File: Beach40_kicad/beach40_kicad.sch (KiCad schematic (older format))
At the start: 75 parts, among them K1 RELAY_2RT, P1 LO In, P2 Mic In, P3 Audio Out, P4 ANT, Q1 BC548, Q2 2N2222, Q3 BD139, Q4 BD139, U1 LM386

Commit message: - slight fixes, working on 2 computers now!
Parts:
- C1, C20, C21, C23, C3, C4, C8: footprint FT:1210_CAP -> Capacitors_ThroughHole:Capacitor3MMDiscRM2.5
- C10, C26: footprint (none) -> FT:CAP_ELECTRO_D4S1.8
- C11, C13, C14, C15, C16, C17, C18, C19, C22, C24, C25, C27, C28, C29: footprint (none) -> Capacitors_ThroughHole:Capacitor3MMDiscRM2.5
- C12: value C_POL -> 220u; footprint (none) -> FT:CAP_ELECTRO_D4S1.8
- C2: value CAP -> 100n; footprint FT:1210_CAP -> Capacitors_ThroughHole:Capacitor3MMDiscRM2.5
- C5: value C_POL -> 1u
- C7, C9: footprint FT:1210_CAP -> FT:CAP_ELECTRO_D4S1.8
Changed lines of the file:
@@
 EESchema Schematic File Version 2
-LIBS:freetronics_schematic
 LIBS:sma
 LIBS:power
@@
 LIBS:atmel
 LIBS:contrib
-LIBS:sma_edge
 LIBS:valves
 LIBS:beach40_kicad-cache
@@
 F 0 "C8" H 3250 5850 40  0000 L CNN
 F 1 "10nF" H 3256 5665 40  0000 L CNN
-F 2 "FT:1210_CAP" H 3288 5600 30  0001 C CNN
+F 2 "Capacitors_ThroughHole:Capacitor3MMDiscRM2.5" H 3288 5600 30  0001 C CNN
 F 3 "" H 3250 5750 60  0000 C CNN
 	1    3250 5750
@@
 F 3 "" H 6150 4050 60  0000 C CNN
 	1    6150 4050
-	1    0    0    -1
+	0    -1   -1   0
 $EndComp
 $Comp
@@
 F 3 "" H 6150 3600 60  0000 C CNN
 	1    6150 3600
-	1    0    0    -1
+	0    -1   -1   0
 $EndComp
 Wire Wire Line
@@
 F 0 "C14" H 5400 3700 50  0000 L CNN
 F 1 "100n" H 5400 3500 50  0000 L CNN
-F 2 "" H 5350 3600 60  0001 C CNN
+F 2 "Capacitors_ThroughHole:Capacitor3MMDiscRM2.5" H 5350 3600 60  0001 C CNN
 F 3 "" H 5350 3600 60  0000 C CNN
 	1    5350 3600
@@
 F 0 "C20" H 7000 4300 50  0000 L CNN
 F 1 "100n" H 7000 4100 50  0000 L CNN
-F 2 "FT:1210_CAP" H 6950 4200 60  0001 C CNN
+F 2 "Capacitors_ThroughHole:Capacitor3MMDiscRM2.5" H 6950 4200 60  0001 C CNN
 F 3 "" H 6950 4200 60  0000 C CNN
 	1    6950 4200
@@
 F 0 "C23" H 7850 6000 50  0000 L CNN
 F 1 "100n" H 7850 5800 50  0000 L CNN
-F 2 "FT:1210_CAP" H 7800 5900 60  0001 C CNN
+F 2 "Capacitors_ThroughHole:Capacitor3MMDiscRM2.5" H 7800 5900 60  0001 C CNN
 F 3 "" H 7800 5900 60  0000 C CNN
 	1    7800 5900
@@
 F 3 "" H 7800 4350 60  0000 C CNN
 	1    7800 4350
-	1    0    0    -1
+	0    -1   -1   0
 $EndComp
 $Comp
@@
 F 3 "" H 7800 4000 60  0000 C CNN
 	1    7800 4000
-	1    0    0    -1
+	0    -1   -1   0
 $EndComp
 Wire Wire Line
@@
 F 0 "C21" H 7400 3800 50  0000 L CNN
 F 1 "100n" H 7400 3600 50  0000 L CNN
-F 2 "FT:1210_CAP" H 7350 3700 60  0001 C CNN
+F 2 "Capacitors_ThroughHole:Capacitor3MMDiscRM2.5" H 7350 3700 60  0001 C CNN
 F 3 "" H 7350 3700 60  0000 C CNN
 	1    7350 3700
@@
 F 0 "C15" H 5400 4550 50  0000 L CNN
 F 1 "1n" H 5400 4350 50  0000 L CNN
-F 2 "" H 5350 4450 60  0001 C CNN
+F 2 "Capacitors_ThroughHole:Capacitor3MMDiscRM2.5" H 5350 4450 60  0001 C CNN
 F 3 "" H 5350 4450 60  0000 C CNN
 	1    5350 4450
@@
 F 0 "C3" H 2350 5100 50  0000 L CNN
 F 1 "10n" H 2350 4900 50  0000 L CNN
-F 2 "FT:1210_CAP" H 2300 5000 60  0001 C CNN
+F 2 "Capacitors_ThroughHole:Capacitor3MMDiscRM2.5" H 2300 5000 60  0001 C CNN
 F 3 "" H 2300 5000 60  0000 C CNN
 	1    2300 5000
@@
 F 0 "C16" H 5700 5000 50  0000 L CNN
 F 1 "100n" H 5700 4800 50  0000 L CNN
-F 2 "" H 5650 4900 60  0001 C CNN
+F 2 "Capacitors_ThroughHole:Capacitor3MMDiscRM2.5" H 5650 4900 60  0001 C CNN
 F 3 "" H 5650 4900 60  0000 C CNN
 	1    5650 4900
@@
 F 0 "C17" H 6650 6150 50  0000 L CNN
 F 1 "100n" H 6650 5950 50  0000 L CNN
-F 2 "" H 6600 6050 60  0001 C CNN
+F 2 "Capacitors_ThroughHole:Capacitor3MMDiscRM2.5" H 6600 6050 60  0001 C CNN
 F 3 "" H 6600 6050 60  0000 C CNN
 	1    6600 6050
@@
 F 0 "C25" H 8350 4300 50  0000 L CNN
 F 1 "100n" H 8350 4100 50  0000 L CNN
-F 2 "" H 8300 4200 60  0001 C CNN
+F 2 "Capacitors_ThroughHole:Capacitor3MMDiscRM2.5" H 8300 4200 60  0001 C CNN
 F 3 "" H 8300 4200 60  0000 C CNN
 	1    8300 4200
@@
 F 3 "" H 8900 3800 60  0000 C CNN
 	1    8900 3800
-	0    1    1    0
+	-1   0    0    1
 $EndComp
 Wire Wire Line
@@
 F 0 "C29" H 9400 4200 50  0000 L CNN
 F 1 "100n" H 9400 4000 50  0000 L CNN
-F 2 "" H 9350 4100 60  0001 C CNN
+F 2 "Capacitors_ThroughHole:Capacitor3MMDiscRM2.5" H 9350 4100 60  0001 C CNN
 F 3 "" H 9350 4100 60  0000 C CNN
 	1    9350 4100
@@
 F 0 "C26" H 8600 3600 50  0000 L CNN
 F 1 "220u" H 8600 3400 50  0000 L CNN
-F 2 "" H 8550 3500 60  0001 C CNN
+F 2 "FT:CAP_ELECTRO_D4S1.8" H 8550 3500 60  0001 C CNN
 F 3 "" H 8550 3500 60  0000 C CNN
 	1    8550 3500
@@
 F 3 "" H 7250 2150 60  0000 C CNN
 	1    7250 2150
-	1    0    0    -1
+	0    -1   -1   0
 $EndComp
 $Comp
@@
 F 3 "" H 7900 2150 60  0000 C CNN
 	1    7900 2150
-	1    0    0    -1
+	0    -1   -1   0
 $EndComp
 $Comp
@@
 F 3 "" H 8550 2150 60  0000 C CNN
 	1    8550 2150
-	1    0    0    -1
+	0    -1   -1   0
 $EndComp
 Text GLabel 6800 2150 0    60   Input ~ 0
@@
 F 0 "C19" H 7000 2550 50  0000 L CNN
 F 1 "220p" H 7000 2350 50  0000 L CNN
-F 2 "" H 6950 2450 60  0001 C CNN
+F 2 "Capacitors_ThroughHole:Capacitor3MMDiscRM2.5" H 6950 2450 60  0001 C CNN
 F 3 "" H 6950 2450 60  0000 C CNN
 	1    6950 2450
@@
 F 0 "C18" H 6750 2550 50  0000 L CNN
 F 1 "220p" H 6750 2350 50  0000 L CNN
-F 2 "" H 6700 2450 60  0001 C CNN
+F 2 "Capacitors_ThroughHole:Capacitor3MMDiscRM2.5" H 6700 2450 60  0001 C CNN
 F 3 "" H 6700 2450 60  0000 C CNN
 	1    6700 2450
@@
 F 0 "C22" H 7500 2550 50  0000 L CNN
 F 1 "820p" H 7500 2350 50  0000 L CNN
-F 2 "" H 7450 2450 60  0001 C CNN
+F 2 "Capacitors_ThroughHole:Capacitor3MMDiscRM2.5" H 7450 2450 60  0001 C CNN
 F 3 "" H 7450 2450 60  0000 C CNN
 	1    7450 2450
@@
 F 0 "C24" H 8100 2550 50  0000 L CNN
 F 1 "820p" H 8100 2350 50  0000 L CNN
-F 2 "" H 8050 2450 60  0001 C CNN
+F 2 "Capacitors_ThroughHole:Capacitor3MMDiscRM2.5" H 8050 2450 60  0001 C CNN
 F 3 "" H 8050 2450 60  0000 C CNN
 	1    8050 2450
@@
 F 0 "C27" H 8800 2550 50  0000 L CNN
 F 1 "220p" H 8800 2350 50  0000 L CNN
-F 2 "" H 8750 2450 60  0001 C CNN
+F 2 "Capacitors_ThroughHole:Capacitor3MMDiscRM2.5" H 8750 2450 60  0001 C CNN
 F 3 "" H 8750 2450 60  0000 C CNN
 	1    8750 2450
@@
 F 0 "C28" H 9100 2550 50  0000 L CNN
 F 1 "220p" H 9100 2350 50  0000 L CNN
-F 2 "" H 9050 2450 60  0001 C CNN
+F 2 "Capacitors_ThroughHole:Capacitor3MMDiscRM2.5" H 9050 2450 60  0001 C CNN
 F 3 "" H 9050 2450 60  0000 C CNN
 	1    9050 2450
@@
 F 3 "" H 8550 1700 60  0000 C CNN
 	1    8550 1700
-	1    0    0    -1
+	0    -1   -1   0
 $EndComp
 Wire Wire Line
@@
 F 0 "C7" H 3200 1700 50  0000 L CNN
 F 1 "4.7u" H 3200 1500 50  0000 L CNN
-F 2 "FT:1210_CAP" H 3150 1600 60  0001 C CNN
+F 2 "FT:CAP_ELECTRO_D4S1.8" H 3150 1600 60  0001 C CNN
 F 3 "" H 3150 1600 60  0000 C CNN
 	1    3150 1600
@@
 F 0 "C11" H 4250 2500 50  0000 L CNN
 F 1 "4.7n" H 4250 2300 50  0000 L CNN
-F 2 "" H 4200 2400 60  0001 C CNN
+F 2 "Capacitors_ThroughHole:Capacitor3MMDiscRM2.5" H 4200 2400 60  0001 C CNN
 F 3 "" H 4200 2400 60  0000 C CNN
 	1    4200 2400
@@
 F 0 "C13" H 4950 3200 50  0000 L CNN
 F 1 "100n" H 4950 3000 50  0000 L CNN
-F 2 "" H 4900 3100 60  0001 C CNN
+F 2 "Capacitors_ThroughHole:Capacitor3MMDiscRM2.5" H 4900 3100 60  0001 C CNN
 F 3 "" H 4900 3100 60  0000 C CNN
 	1    4900 3100
@@
 F 0 "C9" H 3750 1000 50  0000 L CNN
 F 1 "220u" H 3750 800 50  0000 L CNN
-F 2 "FT:1210_CAP" H 3700 900 60  0001 C CNN
+F 2 "FT:CAP_ELECTRO_D4S1.8" H 3700 900 60  0001 C CNN
 F 3 "" H 3700 900 60  0000 C CNN
 	1    3700 900
@@
 F 0 "C10" H 4250 1500 50  0000 L CNN
 F 1 "220u" H 4250 1300 50  0000 L CNN
-F 2 "" H 4200 1400 60  0001 C CNN
+F 2 "FT:CAP_ELECTRO_D4S1.8" H 4200 1400 60  0001 C CNN
 F 3 "" H 4200 1400 60  0000 C CNN
 	1    4200 1400
@@
 P 4700 1900
 F 0 "C12" H 4750 2000 50  0000 L CNN
-F 1 "C_POL" H 4750 1800 50  0000 L CNN
-F 2 "" H 4700 1900 60  0001 C CNN
+F 1 "220u" H 4750 1800 50  0000 L CNN
+F 2 "FT:CAP_ELECTRO_D4S1.8" H 4700 1900 60  0001 C CNN
 F 3 "" H 4700 1900 60  0000 C CNN
 	1    4700 1900
@@
 P 2800 1600
 F 0 "C5" H 2850 1700 50  0000 L CNN
-F 1 "C_POL" H 2850 1500 50  0000 L CNN
+F 1 "1u" H 2850 1500 50  0000 L CNN
 F 2 "FT:CAP_ELECTRO_D4S1.8" H 2800 1600 60  0001 C CNN
 F 3 "" H 2800 1600 60  0000 C CNN
@@
 P 2300 2300
 F 0 "C2" H 2350 2400 50  0000 L CNN
-F 1 "CAP" H 2350 2200 50  0000 L CNN
-F 2 "FT:1210_CAP" H 2300 2300 60  0001 C CNN
+F 1 "100n" H 2350 2200 50  0000 L CNN
+F 2 "Capacitors_ThroughHole:Capacitor3MMDiscRM2.5" H 2300 2300 60  0001 C CNN
 F 3 "" H 2300 2300 60  0000 C CNN
 	1    2300 2300
@@
 F 0 "C4" H 2550 2600 50  0000 L CNN
 F 1 "1n" H 2550 2400 50  0000 L CNN
-F 2 "FT:1210_CAP" H 2500 2500 60  0001 C CNN
+F 2 "Capacitors_ThroughHole:Capacitor3MMDiscRM2.5" H 2500 2500 60  0001 C CNN
 F 3 "" H 2500 2500 60  0000 C CNN
 	1    2500 2500
@@
 F 0 "C1" H 2050 1450 50  0000 L CNN
 F 1 "100n" H 2050 1250 50  0000 L CNN
-F 2 "FT:1210_CAP" H 2000 1350 60  0001 C CNN
+F 2 "Capacitors_ThroughHole:Capacitor3MMDiscRM2.5" H 2000 1350 60  0001 C CNN
 F 3 "" H 2000 1350 60  0000 C CNN
 	1    2000 1350

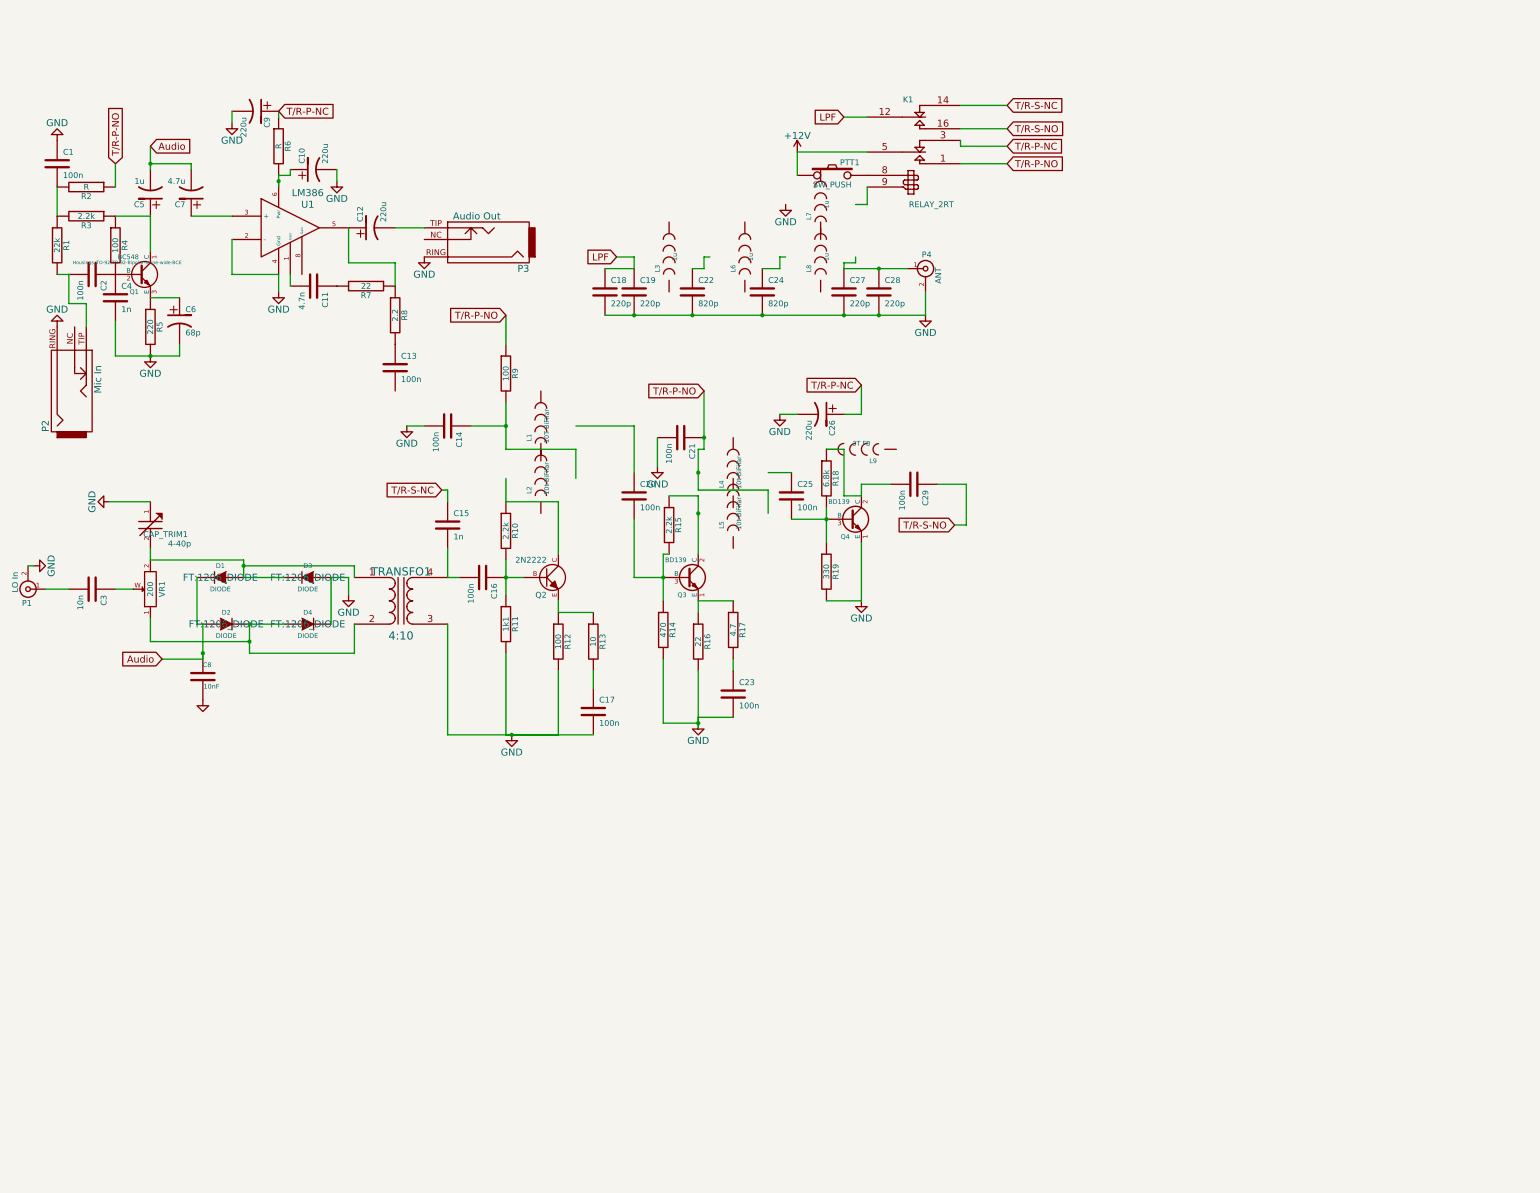
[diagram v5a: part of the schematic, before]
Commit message: VOX added, updated README, Beach40 tweaks.
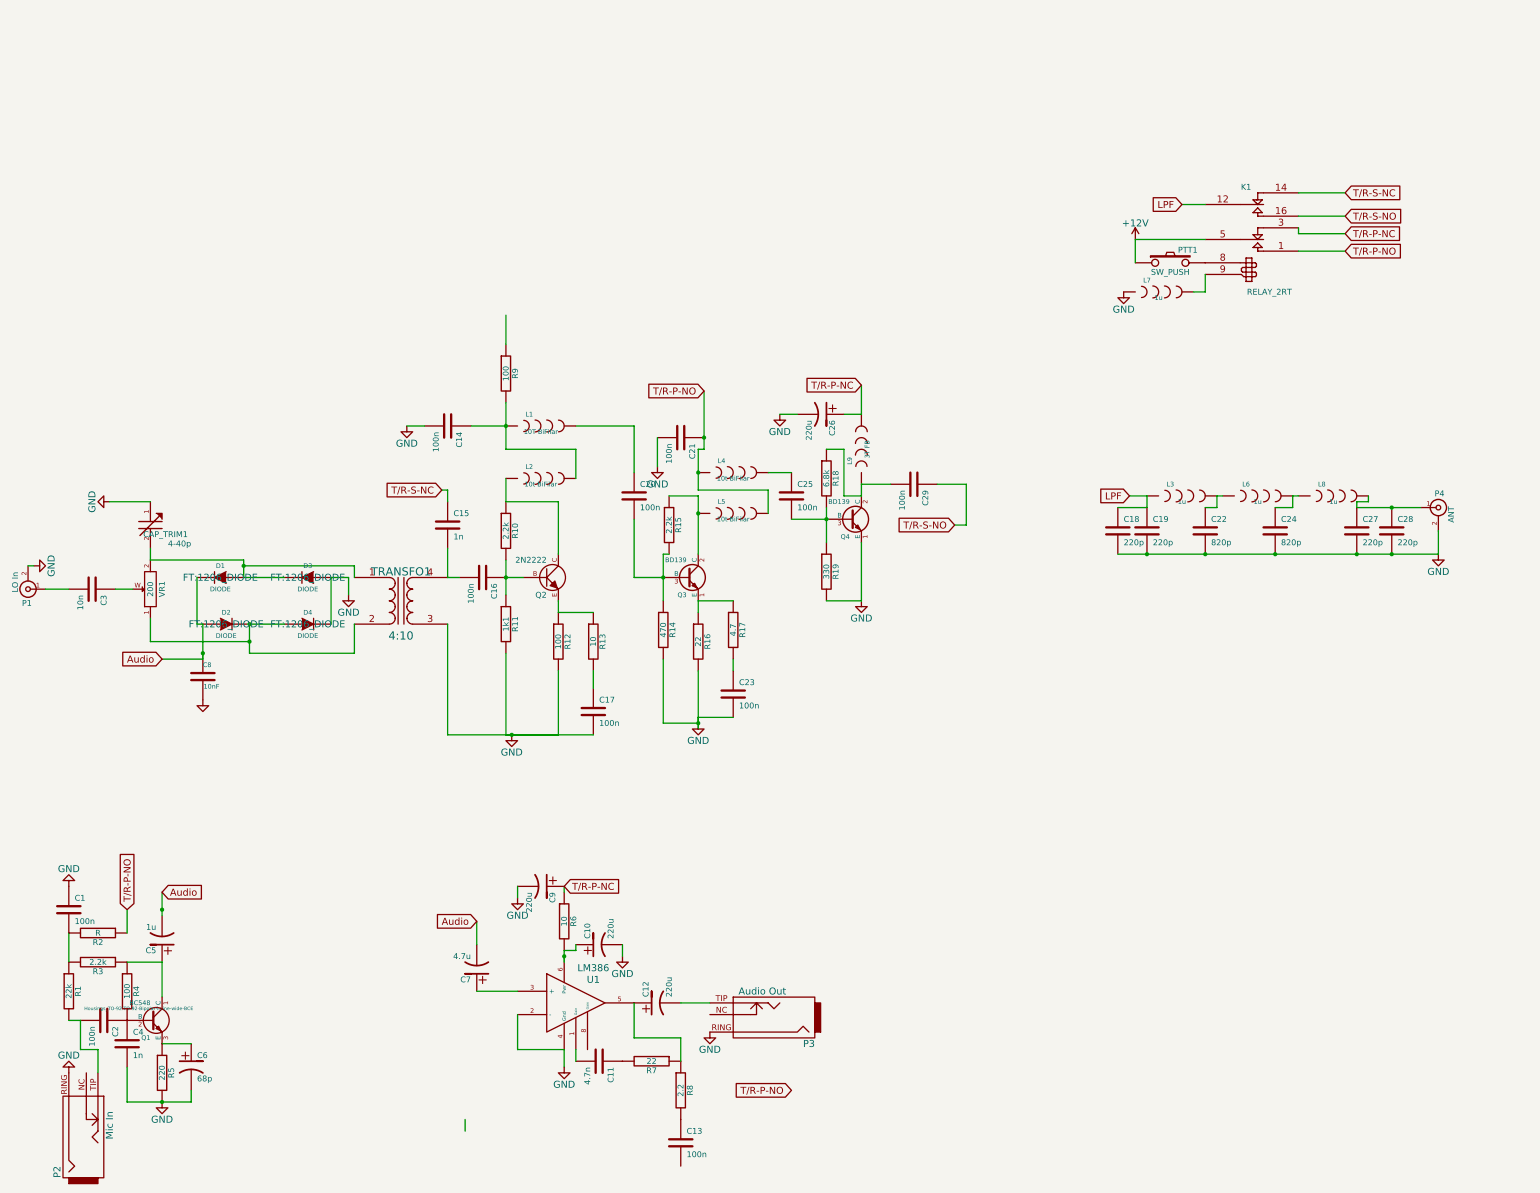
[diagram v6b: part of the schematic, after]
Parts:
- R6: value R -> 10
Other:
- moved on the sheet: C1, C10, C11, C12, C13, C18, C19, C2, C22, C24, C27, C28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
